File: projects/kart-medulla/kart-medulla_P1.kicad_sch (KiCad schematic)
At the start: 67 parts, among them CN1 2601-3103, CN10 2601-3103, CN2 2601-3103, CN3 2601-3103, CN4 2601-3103, CN5 2601-3103, CN6 2601-3103, CN7 2601-3103, CN8 2601-3103, CN9 2601-3103, Q3 IRLZ44NPBF, Q4 BSS123_C5184436, U1 LM358DR, U13 MCP4922-E/SL, U14 MAX4660EUA+T, U19 L7805CDT_C20611927, U23 SSW-122-01-T-D, U24 SSW-122-01-T-S, U25 PCF8574T/3,518, U5 SN74LVC3G17DCTR

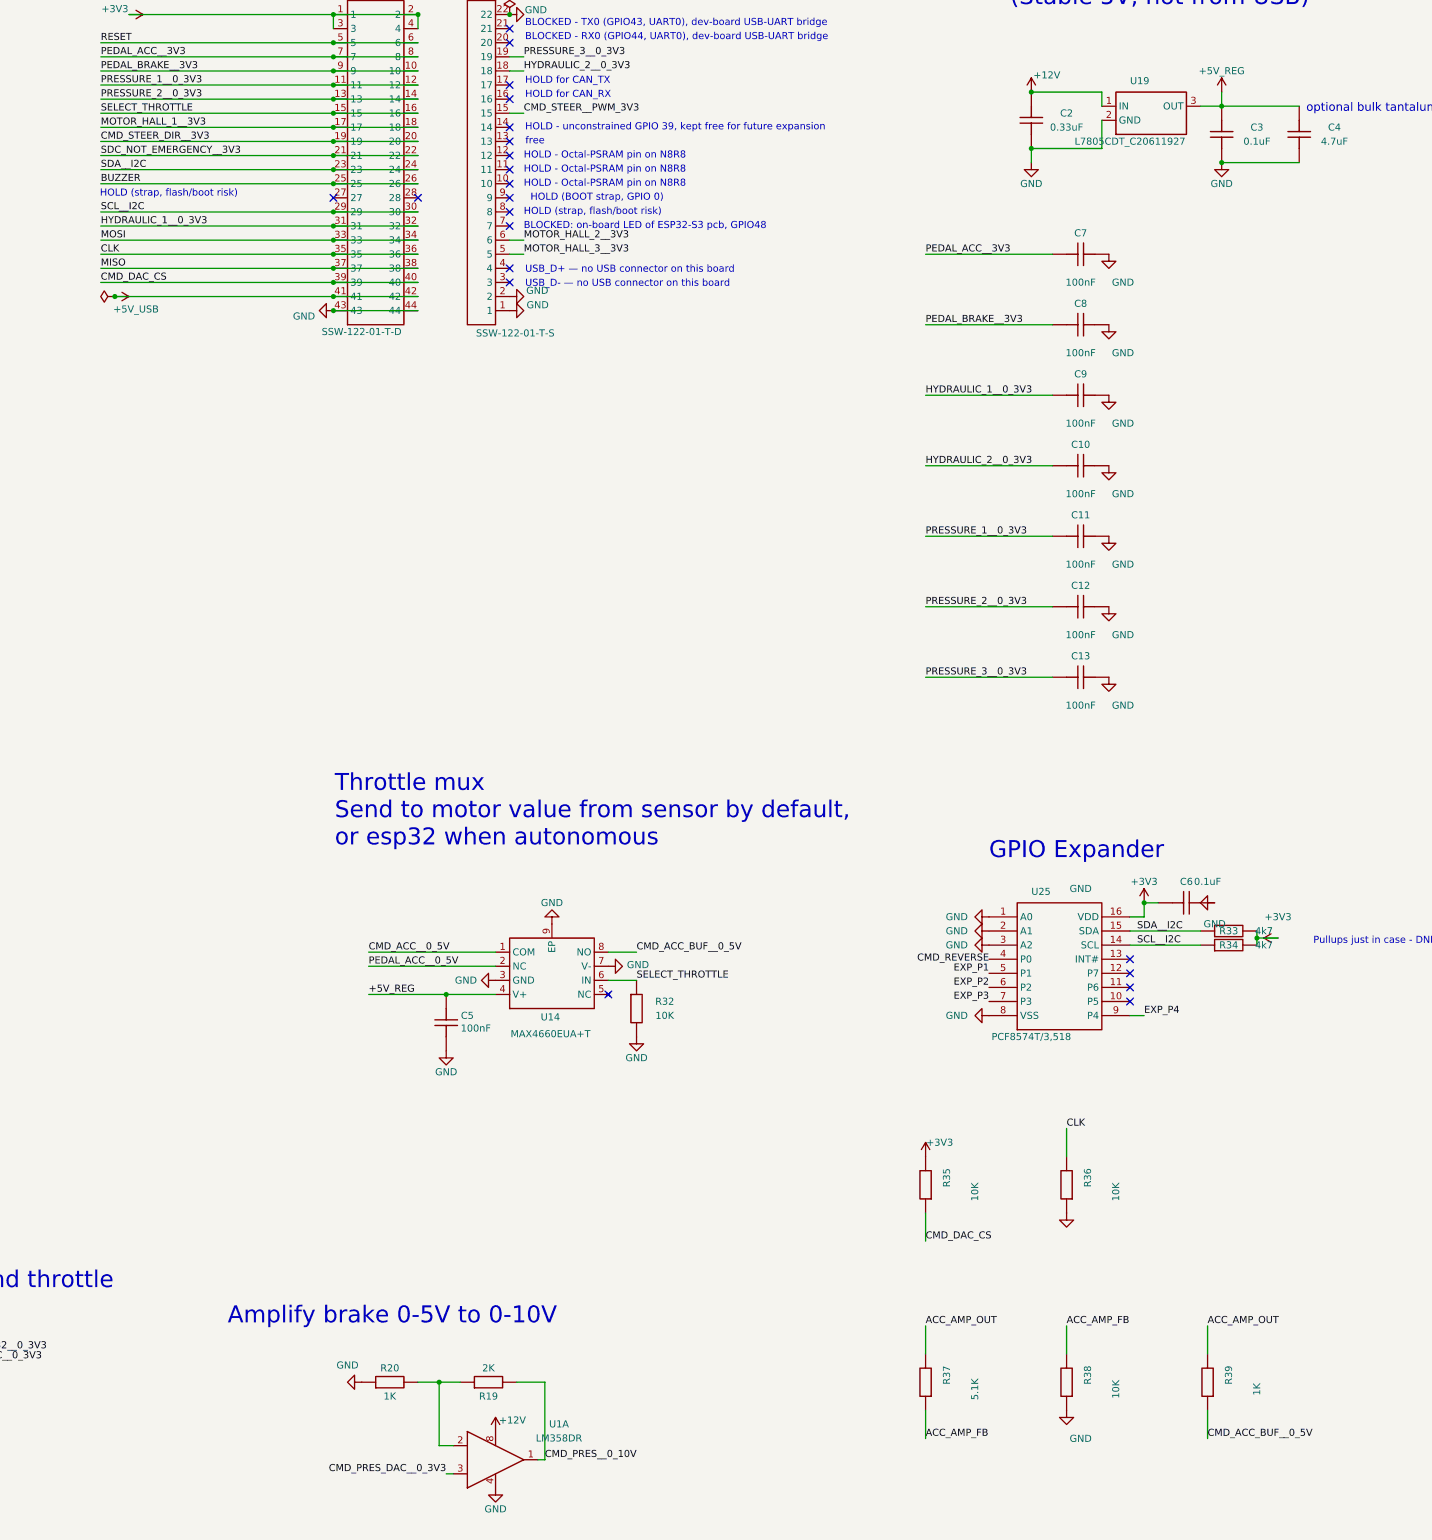
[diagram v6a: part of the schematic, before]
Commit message: delete the throttle mux U14, and bring the docs in line with the board
Removes the MAX4660 (U14), its 10K pulldown R32 and its local 100nF C5 from the schematic. The
mux was a CMOS switch, so with the board unpowered both channel MOSFETs are off and the pedal
was not passed through at all - "normally closed" in the datasheet means closed at logic 0 with
power applied. The kart's panel DPDT switch already selects the throttle source downstream on
metal contacts that work unpowered, so the mux was a second selector in series doing a job that
was already done, by a part that does it worse.

Netlist after the edit: CMD_ACC__0_5V is CN10.1 + R39.1, PEDAL_ACC__0_5V is CN6.2 + R14.2, and
+5V_REG is C3.2 + C4.2 + CN2.3 + U19.3. Deleting C5 was right - it was U14's local decoupling,
and the L7805 keeps C2 0.33uF in with C3 0.1uF and C4 4.7uF out, which meets the datasheet.

ESP32 socket pins U23.15 and U23.16 carried SELECT_THROTTLE and were left dangling, which is 2
ERC errors. Both now have no-connect markers at the same x-coordinates as the existing spare
pair one row down, plus a graphic text note marking GPIO 15 as spare and saying what freed it.
ERC 0 violations.

Documentation brought in line, since the mux is described in several places as fitted:
pinout-esp32-s3.md (pin tables, power-architecture diagram, the whole mux section, the datasheet
list), pinout-cn-connectors.md CN10 row, and parts.md. The MAX4660 section in parts.md is kept
rather than deleted, headed as no longer in the design, because the part is fitted on the
fabricated v1 board and the symbol/footprint/3D sourcing stays useful for anyone working on it.

Two stale claims found while checking and fixed with values read from the netlist rather than
from the prose: parts.md still described U1A as gain 2 with R19 = 1k, and still had the MCP4922
VDD and VREF pins on +5V_REG with a 4.96 V full scale and a -0.3 to +5.3 V absolute maximum.
U13 pins 1, 9, 11 and 13 are all on +3V3, so full scale is 3.26 V typic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
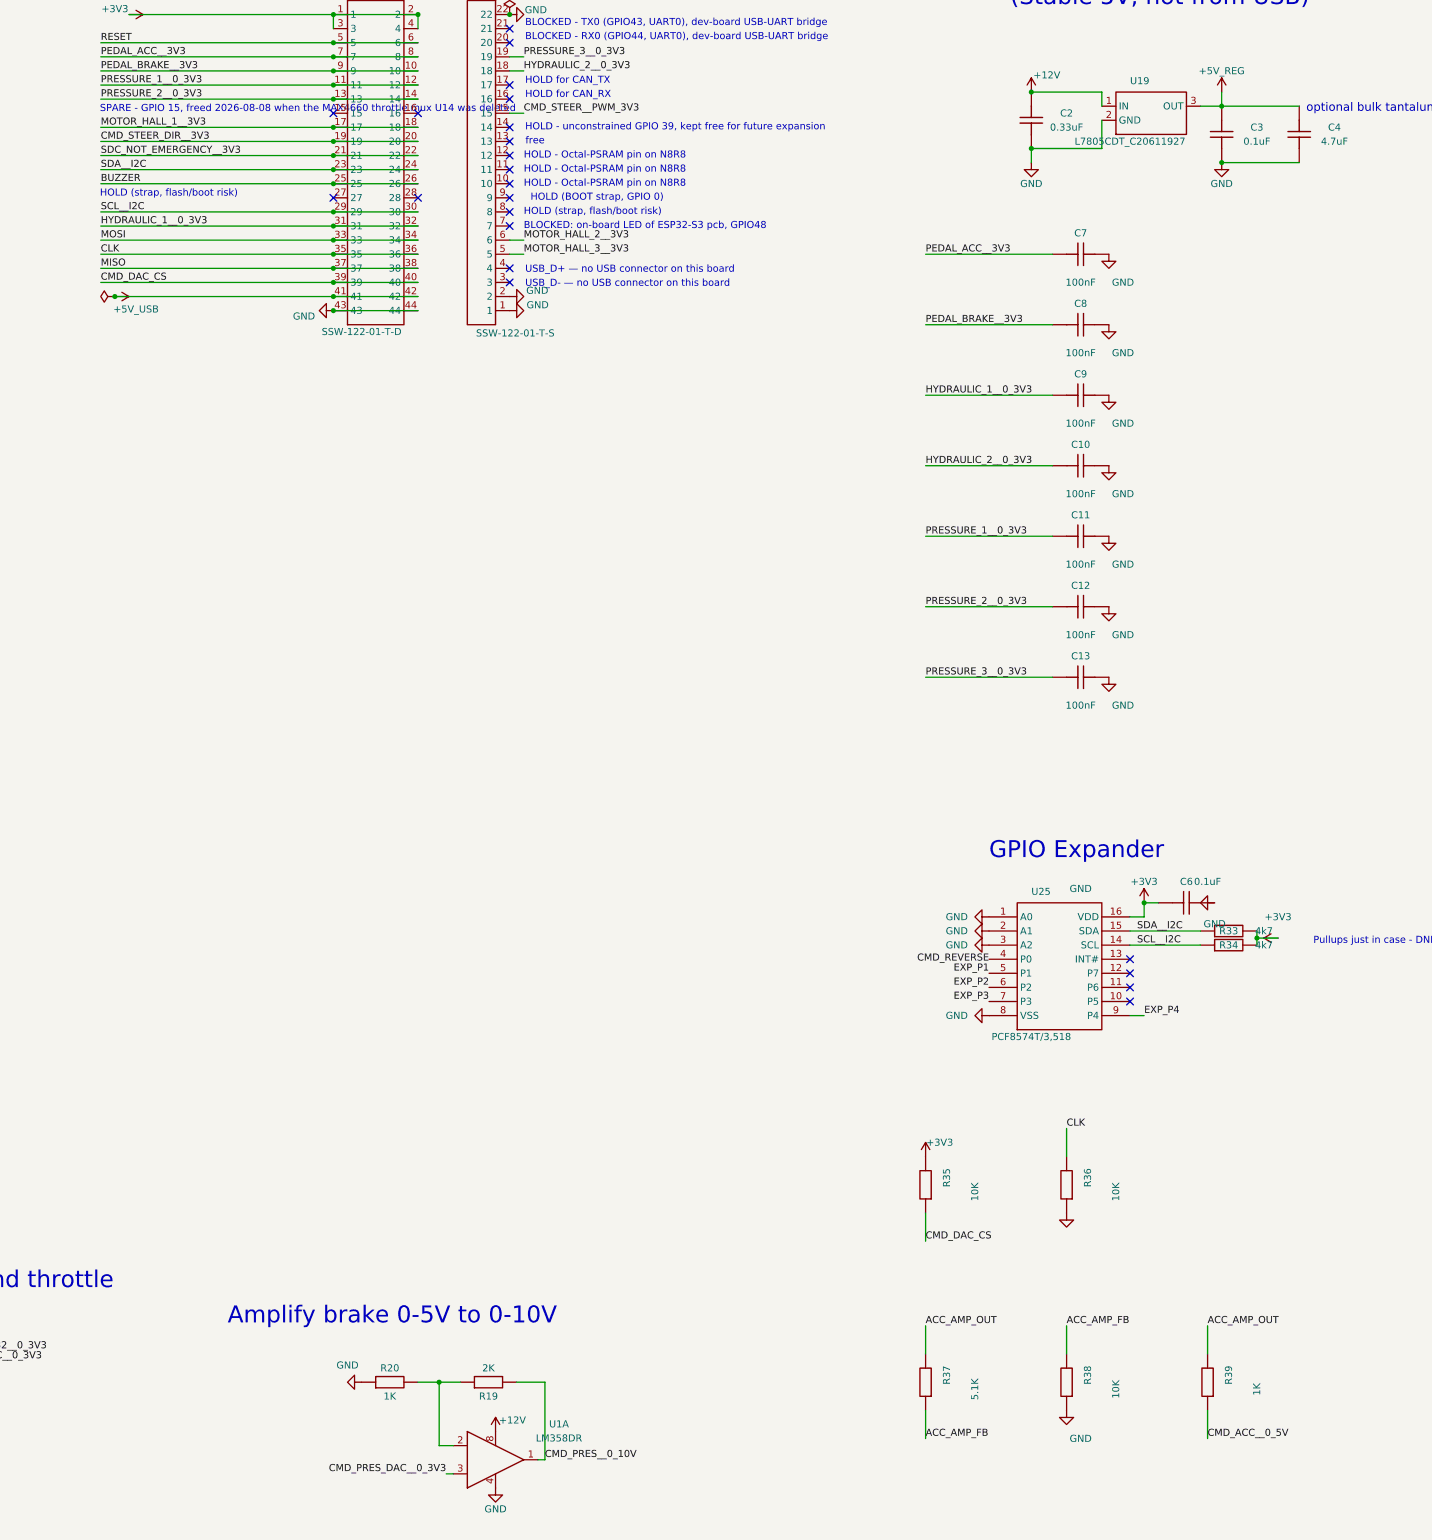
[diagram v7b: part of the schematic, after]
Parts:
- removed C5: 100nF, kart-medulla:C0603, symbol kart-medulla:CAP
- removed R32: 10K, kart-medulla:R0603, symbol kart-medulla:Res
- removed U14: MAX4660EUA+T, kart-medulla:SOP65P490X110-9N, symbol kart-medulla:MAX4660EUA_T
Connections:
- net CMD_ACC_BUF__0_5V is gone; now on net CMD_ACC__0_5V: R39.1
- net SELECT_THROTTLE: no longer names the net of U23.15
- net SELECT_THROTTLE: no longer U23.16
- no-connect marks 24 -> 25
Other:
- note added: "SPARE - GPIO 15, freed 2026-08-08 when the MAX4660 throttle mux U14 was deleted"
- note removed: "Throttle mux Send to motor value from sensor by default, or esp32 when autonomous"

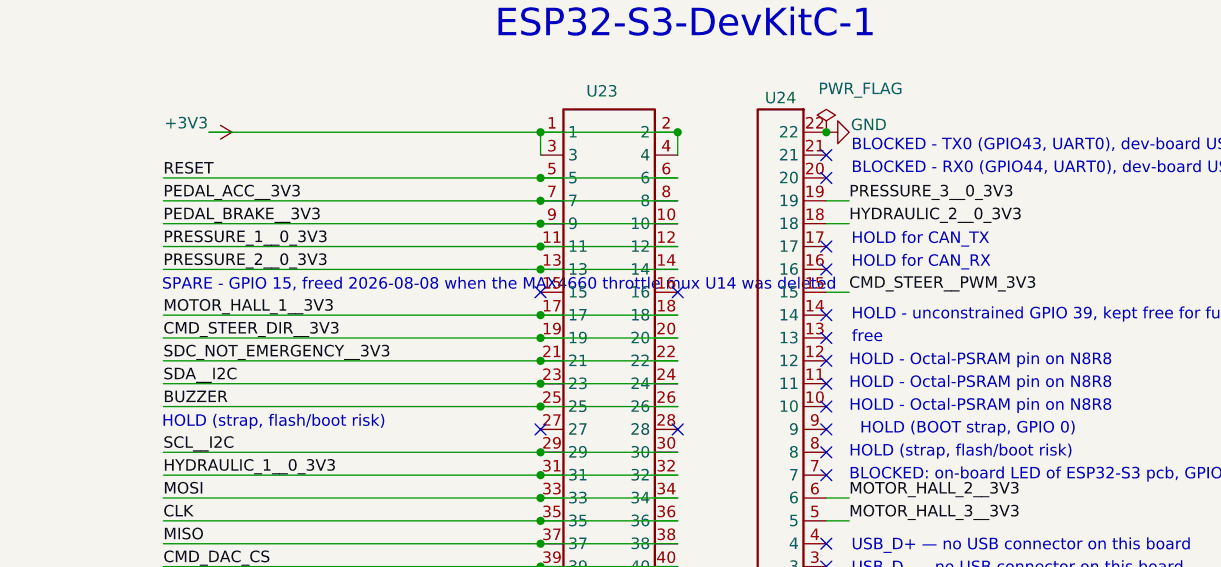
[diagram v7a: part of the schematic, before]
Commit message: shorten the GPIO 15 spare note so it stops overrunning the socket symbol
The note read "SPARE - GPIO 15, freed 2026-08-08 when the MAX4660 throttle mux U14 was deleted",
which drew straight across U23 and collided with the annotations in the next column. It is now
"SPARE (was mux select)", shorter than the neighbouring "HOLD (strap, flash/boot risk)" so it
stays clear. The full reason lives in parts.md and docs/pinout-esp32-s3.md, which is where a
schematic annotation should point rather than carrying the explanation itself.
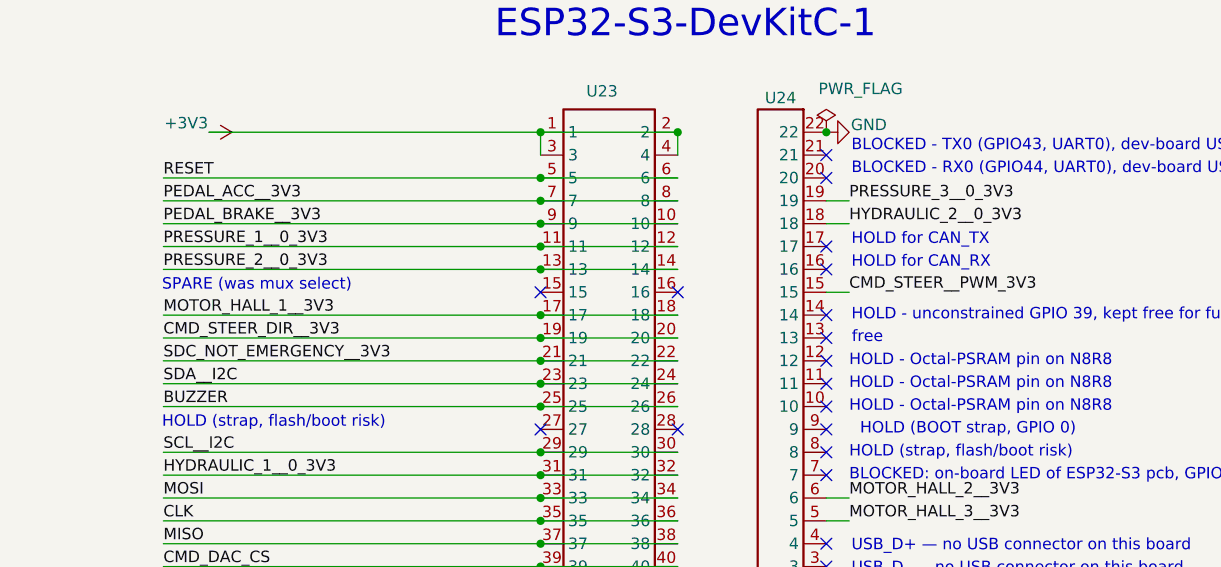
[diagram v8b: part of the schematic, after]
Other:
- note added: "SPARE (was mux select)"
- note removed: "SPARE - GPIO 15, freed 2026-08-08 when the MAX4660 throttle mux U14 was deleted"
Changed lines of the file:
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@@
 		)
 	)
-	(text "SPARE - GPIO 15, freed 2026-08-08 when the MAX4660 throttle mux U14 was deleted"
+	(text "SPARE (was mux select)"
 		(exclude_from_sim no)
 		(at 313.5376 63.5 0)
